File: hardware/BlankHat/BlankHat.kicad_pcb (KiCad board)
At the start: 2 copper layers, 38.1 x 101.6 mm, 6 parts, among them J1 Conn_01x08_Socket, J2 Conn_01x08_Socket, J3 Conn_01x08_Socket, U1 74HC688, U2 74HC245, U3 74HC245

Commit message: started working on blank smd hat:
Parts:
- added Q1: PZT2222A, Package_TO_SOT_SMD:SOT-223-3_TabPin2, F.Cu at (70.0, 88.9)
- added R1: 1k, Resistor_SMD:R_0201_0603Metric, F.Cu at (59.9, 87.4)
- added R2: 1k, Resistor_SMD:R_0201_0603Metric, F.Cu at (59.9, 89.2)
- J1, J2, J3: moved to B.Cu
- U1, U2, U3: footprint Package_DIP:DIP-20_W7.62mm -> Package_SO:TSSOP-20_4.4x6.5mm_P0.65mm; moved to B.Cu
- moved U1 40.8 mm to (70.0, 108.1)
- moved J1 34.6 mm to (78.7, 120.9)
- moved U3 14.4 mm to (77.8, 64.4)
- moved U2 11.4 mm to (63.1, 64.3)
- turned J2 to 180 degrees
- turned J3 to 0 degrees
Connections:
- J1 pad 7: I5 -> RESP
- U2 pad 11: D6 -> D0
- U2 pad 12: D5 -> D1
- U2 pad 13: D4 -> D2
- U2 pad 15: D2 -> D4
- U2 pad 16: D1 -> D5
- U2 pad 17: D0 -> D6
- U2 pad 18: Net-(J2-Pin_1) -> D7
- U2 pad 2: +5V -> Net-(J2-Pin_1)
- U3 pad 11: D14 -> D8
- U3 pad 12: D13 -> D9
- U3 pad 13: D12 -> D10
- U3 pad 15: D10 -> D12
- U3 pad 16: D9 -> D13
- U3 pad 17: D8 -> D14
- U3 pad 18: D7 -> D15
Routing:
- net +5V: track 0.00 -> 53.0 mm
- net GND: track 0.00 -> 34.1 mm
- net I5: track 0.00 -> 20.4 mm
- net I4: track 0.00 -> 16.0 mm
- net I0: track 0.00 -> 11.5 mm
- net I1: track 0.00 -> 11.0 mm
- net I2: track 0.00 -> 10.5 mm
- net I3: track 0.00 -> 10.0 mm
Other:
- board size 38.1 x 101.6 mm -> 38.1 x 73.8 mm

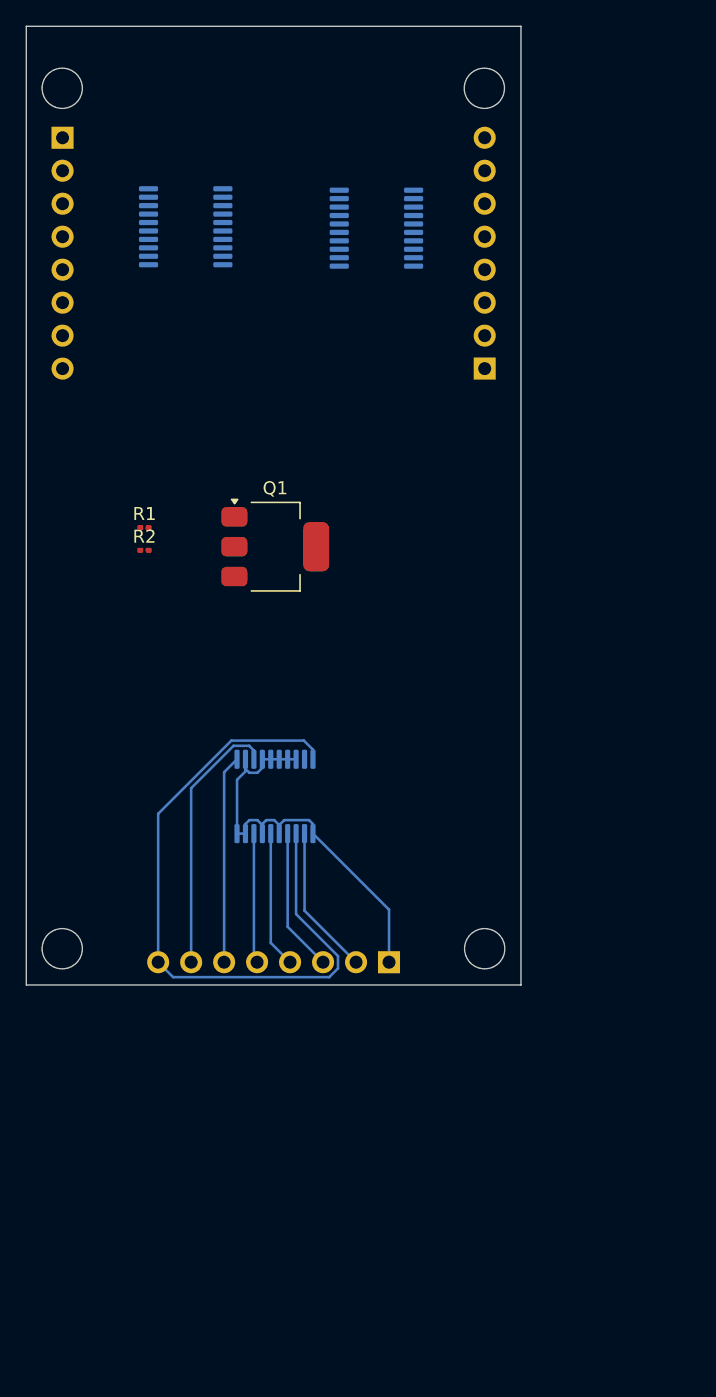
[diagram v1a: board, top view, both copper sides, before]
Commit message: designing new main board
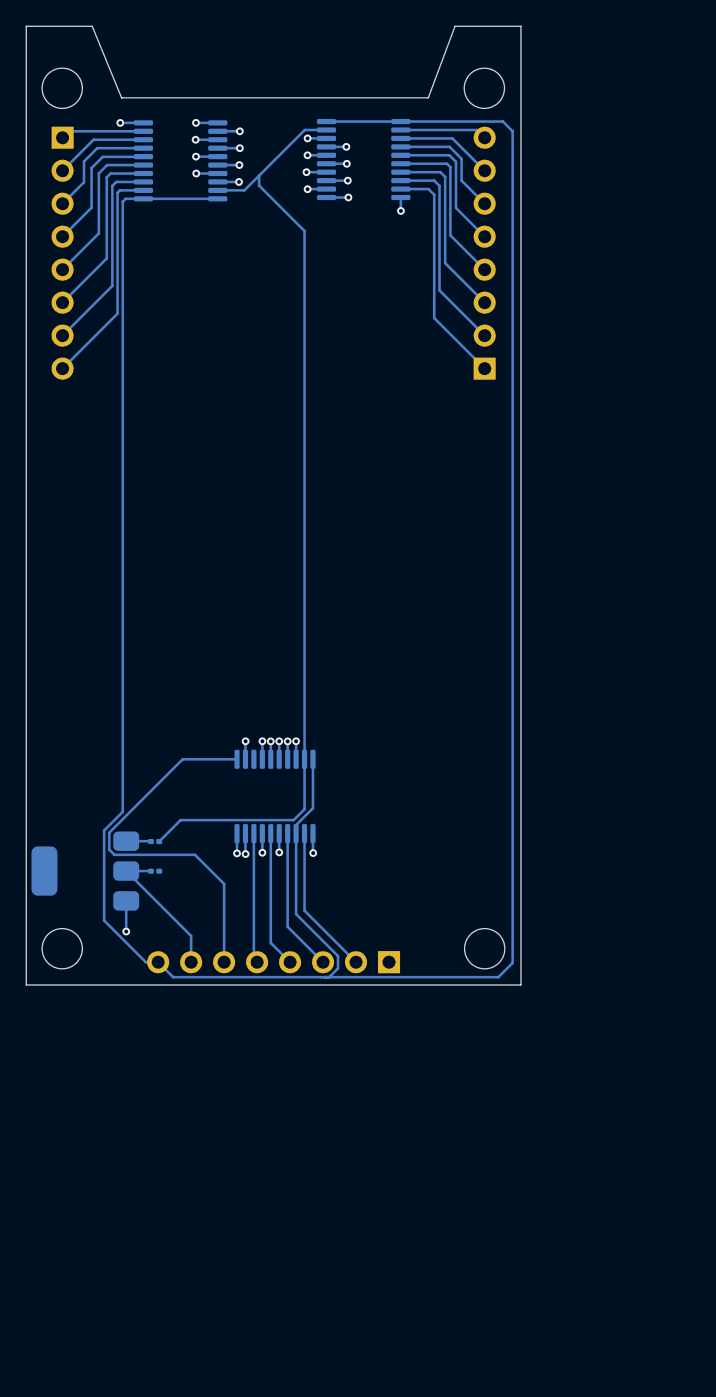
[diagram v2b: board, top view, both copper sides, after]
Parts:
- Q1, R1, R2: moved to B.Cu
- moved Q1 28.9 mm to (55.3, 113.9), turned to 180 degrees
- moved R2 24.7 mm to (60.7, 113.9)
- moved R1 24.2 mm to (60.7, 111.6), turned to 180 degrees
- moved U3 5.38 mm to (76.8, 59.1)
- moved U2 5.09 mm to (62.7, 59.2)
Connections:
- U2 pad 2: Net-(J2-Pin_1) -> Net-(J2-Pin_8)
- U2 pad 3: Net-(J2-Pin_2) -> Net-(J2-Pin_7)
- U2 pad 4: Net-(J2-Pin_3) -> Net-(J2-Pin_6)
- U2 pad 5: Net-(J2-Pin_4) -> Net-(J2-Pin_5)
- U2 pad 6: Net-(J2-Pin_5) -> Net-(J2-Pin_4)
- U2 pad 7: Net-(J2-Pin_6) -> Net-(J2-Pin_3)
- U2 pad 8: Net-(J2-Pin_7) -> Net-(J2-Pin_2)
- U2 pad 9: Net-(J2-Pin_8) -> Net-(J2-Pin_1)
- U3 pad 2: Net-(J3-Pin_1) -> Net-(J3-Pin_8)
- U3 pad 3: Net-(J3-Pin_2) -> Net-(J3-Pin_7)
- U3 pad 4: Net-(J3-Pin_3) -> Net-(J3-Pin_6)
- U3 pad 5: Net-(J3-Pin_4) -> Net-(J3-Pin_5)
- U3 pad 6: Net-(J3-Pin_5) -> Net-(J3-Pin_4)
- U3 pad 7: Net-(J3-Pin_6) -> Net-(J3-Pin_3)
- U3 pad 8: Net-(J3-Pin_7) -> Net-(J3-Pin_2)
- U3 pad 9: Net-(J3-Pin_8) -> Net-(J3-Pin_1)
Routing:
- net +5V: track 53.0 -> 195.1 mm
- net Net-(U1-P=R): track 0.00 -> 72.8 mm
- net I5: track 20.4 -> 0.00 mm
- net Net-(J3-Pin_1): track 0.00 -> 17.8 mm
- net Net-(J2-Pin_8): track 0.00 -> 17.4 mm
- net Net-(J3-Pin_2): track 0.00 -> 16.1 mm
- net Net-(J2-Pin_7): track 0.00 -> 15.6 mm
- net Net-(J3-Pin_3): track 0.00 -> 14.5 mm
- net Net-(J2-Pin_6): track 0.00 -> 14.0 mm
- net I4: track 16.0 -> 29.4 mm
- net GND: track 34.1 -> 21.1 mm, vias 0 -> 14
- net Net-(J3-Pin_4): track 0.00 -> 12.9 mm
- net Net-(J2-Pin_5): track 0.00 -> 12.3 mm
- net Net-(J3-Pin_5): track 0.00 -> 11.1 mm
- net RESP: track 0.00 -> 11.0 mm
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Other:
- outline, holes or cut-outs redrawn

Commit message: made the blank hat with correct footprint
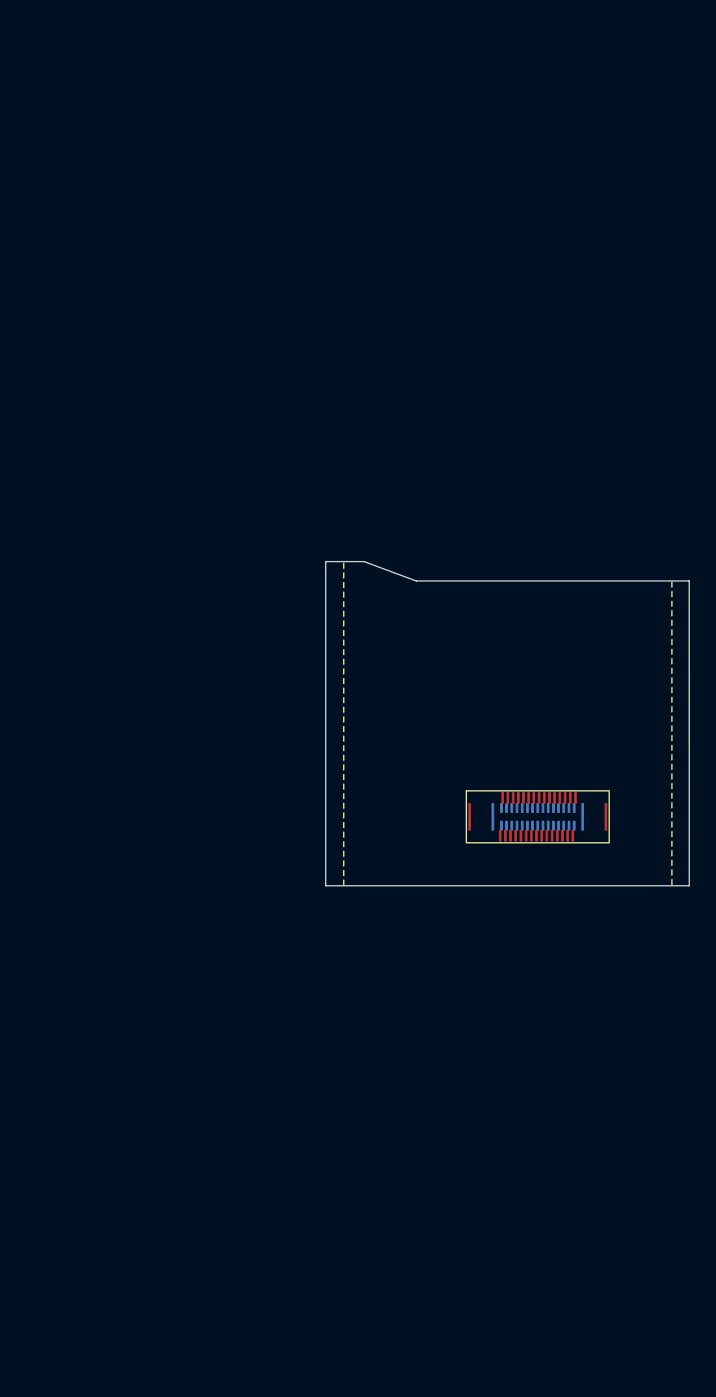
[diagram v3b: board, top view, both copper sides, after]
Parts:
- removed J3: Conn_01x08_Socket, Connector_PinSocket_2.54mm:PinSocket_1x08_P2.54mm_Vertical
- removed Q1: PZT2222A, Package_TO_SOT_SMD:SOT-223-3_TabPin2
- removed R1, R2: 1k, Resistor_SMD:R_0201_0603Metric
- removed U1: 74HC688, Package_SO:TSSOP-20_4.4x6.5mm_P0.65mm
- removed U2, U3: 74HC245, Package_SO:TSSOP-20_4.4x6.5mm_P0.65mm
- J1: value Conn_01x08_Socket -> Conn_02x16_Top_Bottom; footprint Connector_PinSocket_2.54mm:PinSocket_1x08_P2.54mm_Vertical -> MolexFSB:FSB5 Series 0.40 mm Pitch Floating SlimStack Board-to-Board Receptacles
- J2: value Conn_01x08_Socket -> Conn_02x16_Top_Bottom; footprint Connector_PinSocket_2.54mm:PinSocket_1x08_P2.54mm_Vertical -> MolexFSB:FSB5 Series 0.40 mm Pitch Floating SlimStack Board-to-Board Plugs; moved to F.Cu
- moved J2 63.8 mm to (90.2, 109.7), turned to 0 degrees
- moved J1 16.0 mm to (90.2, 109.7), turned to 0 degrees
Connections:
- J1 pad 1: GND -> CONN_0
- J1 pad 2: I0 -> CONN_1
- J1 pad 3: I1 -> CONN_2
- J1 pad 4: I2 -> CONN_3
- J1 pad 5: I3 -> CONN_4
- J1 pad 6: I4 -> CONN_5
- J1 pad 7: RESP -> CONN_6
- J1 pad 8: +5V -> CONN_7
- J2 pad 1: Net-(J2-Pin_1) -> CONN_15
- J2 pad 2: Net-(J2-Pin_2) -> CONN_16
- J2 pad 3: Net-(J2-Pin_3) -> CONN_17
- J2 pad 4: Net-(J2-Pin_4) -> CONN_18
- J2 pad 5: Net-(J2-Pin_5) -> CONN_19
- J2 pad 6: Net-(J2-Pin_6) -> CONN_20
- J2 pad 7: Net-(J2-Pin_7) -> CONN_21
- J2 pad 8: Net-(J2-Pin_8) -> CONN_22
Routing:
- net +5V: track 195.1 -> 0.00 mm
- net Net-(U1-P=R): track 72.8 -> 0.00 mm
- net I4: track 29.4 -> 0.00 mm
- net GND: track 21.1 -> 0.00 mm, vias 14 -> 0
- net Net-(J3-Pin_1): track 17.8 -> 0.00 mm
- net Net-(J2-Pin_8): track 17.4 -> 0.00 mm
- net Net-(J3-Pin_2): track 16.1 -> 0.00 mm
- net Net-(J2-Pin_7): track 15.6 -> 0.00 mm
- net Net-(J3-Pin_3): track 14.5 -> 0.00 mm
- net Net-(J2-Pin_6): track 14.0 -> 0.00 mm
- net Net-(J3-Pin_4): track 12.9 -> 0.00 mm
- net Net-(J2-Pin_5): track 12.3 -> 0.00 mm
- net I0: track 11.5 -> 0.00 mm
- net Net-(J3-Pin_5): track 11.1 -> 0.00 mm
- net I1: track 11.0 -> 0.00 mm
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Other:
- board size 38.1 x 73.8 mm -> 28 x 25 mm
